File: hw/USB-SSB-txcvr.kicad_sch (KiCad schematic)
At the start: 0 parts

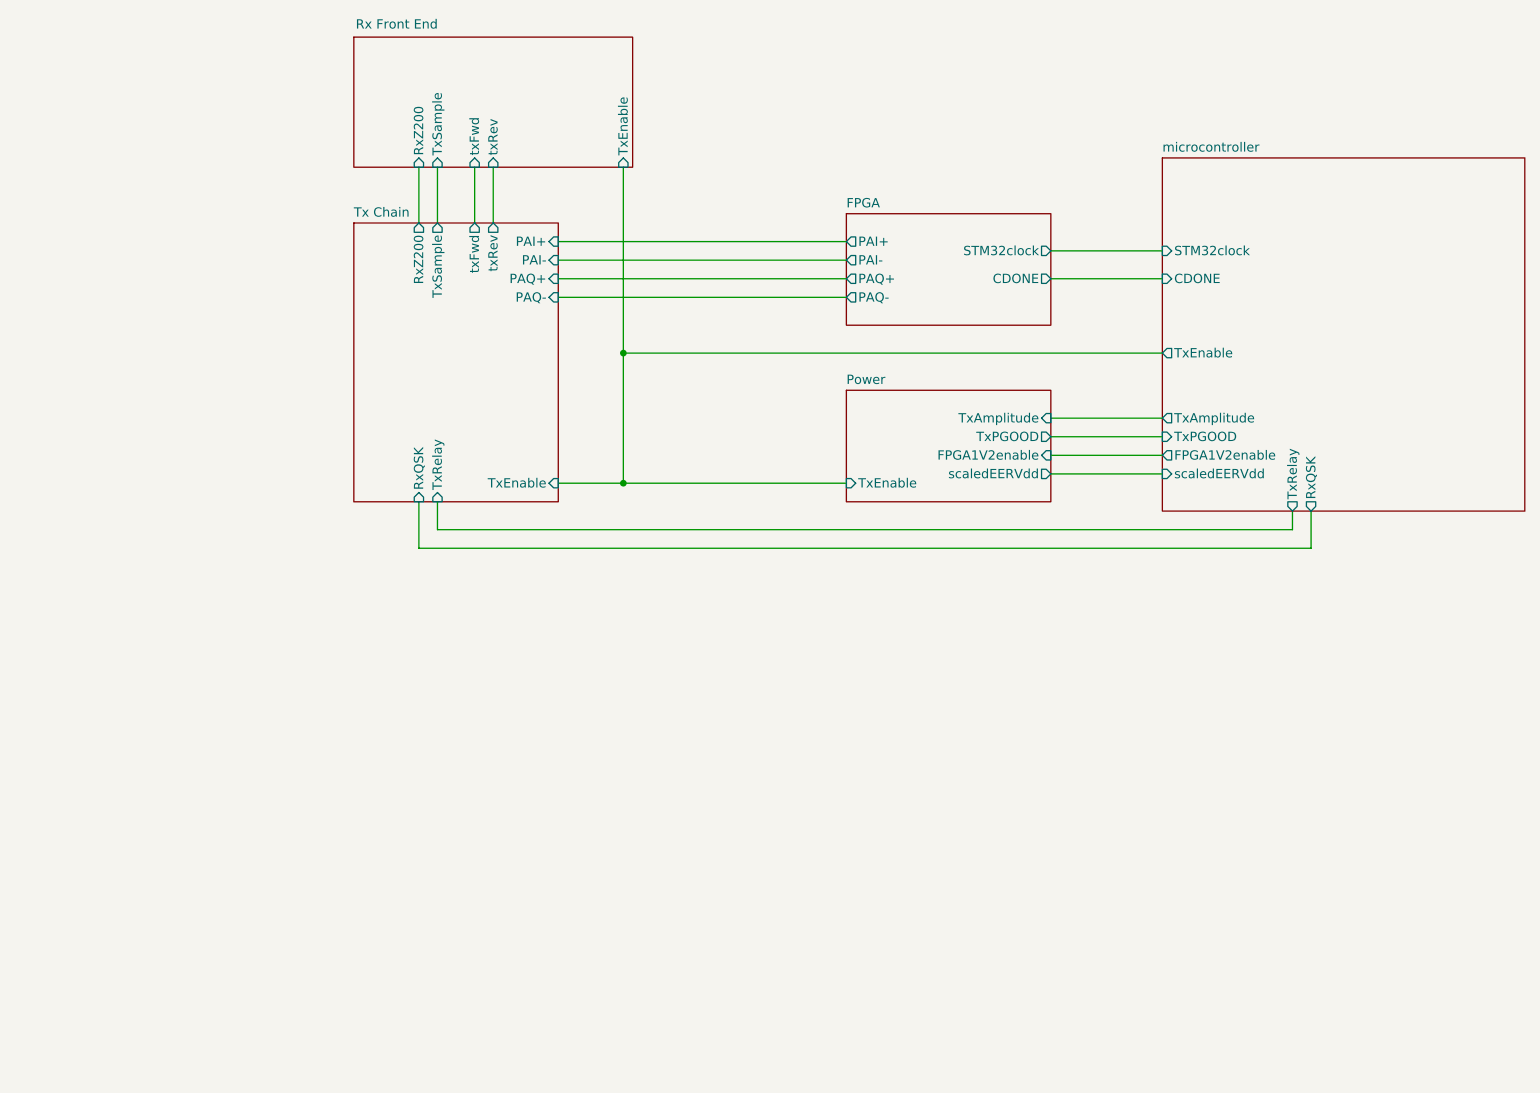
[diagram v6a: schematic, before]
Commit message: Massive (simple) fixes to connect Ctrl bus across sheets - I had misunderstood how that works.
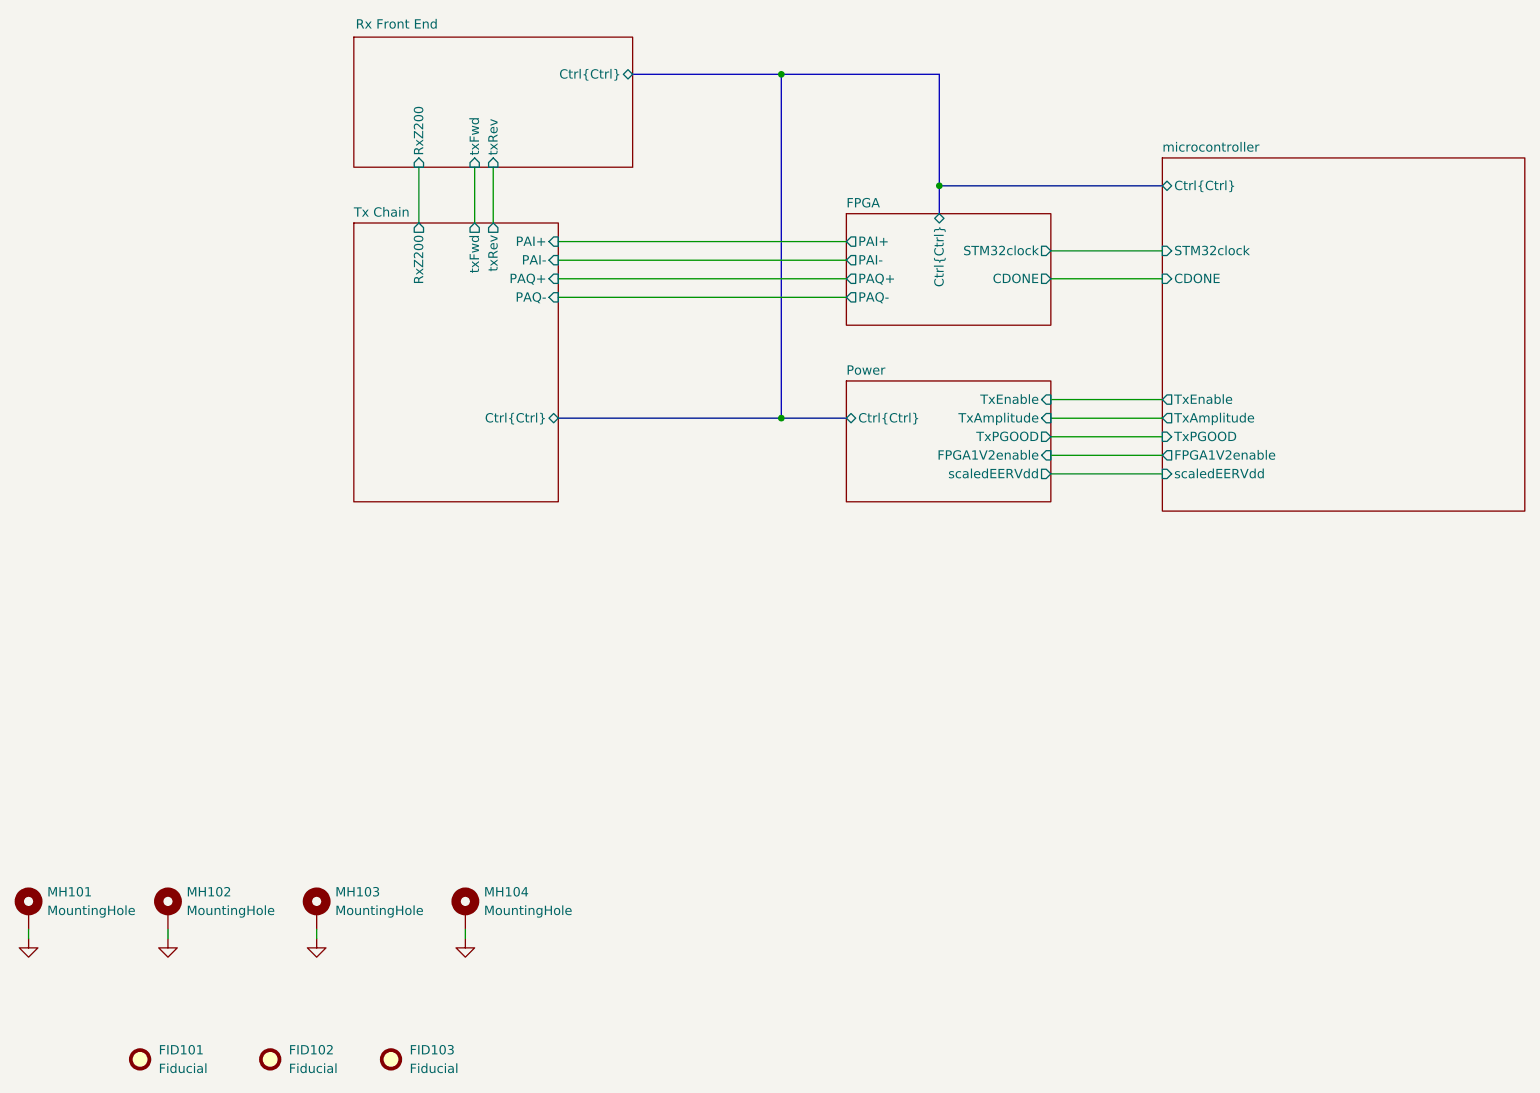
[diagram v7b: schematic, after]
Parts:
- added FID101, FID102, FID103: Fiducial, Fiducial:Fiducial_0.5mm_Mask2mm, symbol Mechanical:Fiducial
- added MH101, MH102, MH103, MH104: MountingHole, MountingHole:MountingHole_3.2mm_M3_ISO7380_Pad, symbol Mechanical:MountingHole_Pad
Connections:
- new net GND: MH101.1, MH102.1, MH103.1, MH104.1
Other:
- sheet FPGA ports: added Ctrl{Ctrl}; removed none
- sheet Power ports: added Ctrl{Ctrl}; removed none
- sheet Rx Front End ports: added Ctrl{Ctrl}; removed TxEnable, TxSample
- sheet Tx Chain ports: added Ctrl{Ctrl}; removed RxQSK, TxEnable, TxRelay, TxSample
- sheet microcontroller ports: added Ctrl{Ctrl}; removed RxQSK, TxRelay

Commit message: Started routing again with real board outline. Placement first, then routing, really.
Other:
- sheet FPGA ports: added FPGA{FPGA}; removed none
- sheet microcontroller ports: added FPGA{FPGA}; removed none
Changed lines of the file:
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@@
 			"qsdPh1d" "qsdPh2a" "qsdPh2b" "qsdPh2c" "qsdPh2d" "bruene" "txData" "txBCLK"
 			"txMCLK" "txWCLK" "usbReset" "usbPOK2" "usbPOK3" "usbnALERT" "enable6V"
-			"enFPGASPIVdd" "enFPGAVpp" "nTxRelay"
+			"enFPGASPIVdd" "enFPGAVpp" "nTxRelay" "enFPGAIOVdd" "audioSCL" "audioSDA"
 		)
 	)
@@
 		(pts
 			(xy 106.68 69.85) (xy 146.05 69.85)
+		)
+		(stroke
+			(width 0)
+			(type default)
+		)
+	)
+	(bus
+		(pts
+			(xy 173.99 67.31) (xy 189.23 67.31)
 		)
 		(stroke
@@
 			)
 		)
+		(pin "FPGA{FPGA}" bidirectional
+			(at 173.99 67.31 0)
+			(effects
+				(font
+					(size 1.27 1.27)
+				)
+				(justify right)
+			)
+		)
 		(instances
 			(project "USB-SSB-txcvr"
@@
 			(effects
 				(font
+					(size 1.27 1.27)
+				)
+				(justify left)
+			)
+		)
+		(pin "FPGA{FPGA}" bidirectional
+			(at 189.23 67.31 180)
+			(effects
+				(font
